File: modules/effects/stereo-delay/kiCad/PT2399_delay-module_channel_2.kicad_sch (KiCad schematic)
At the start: 38 parts, among them Q1 2N3904, U2 PT2399

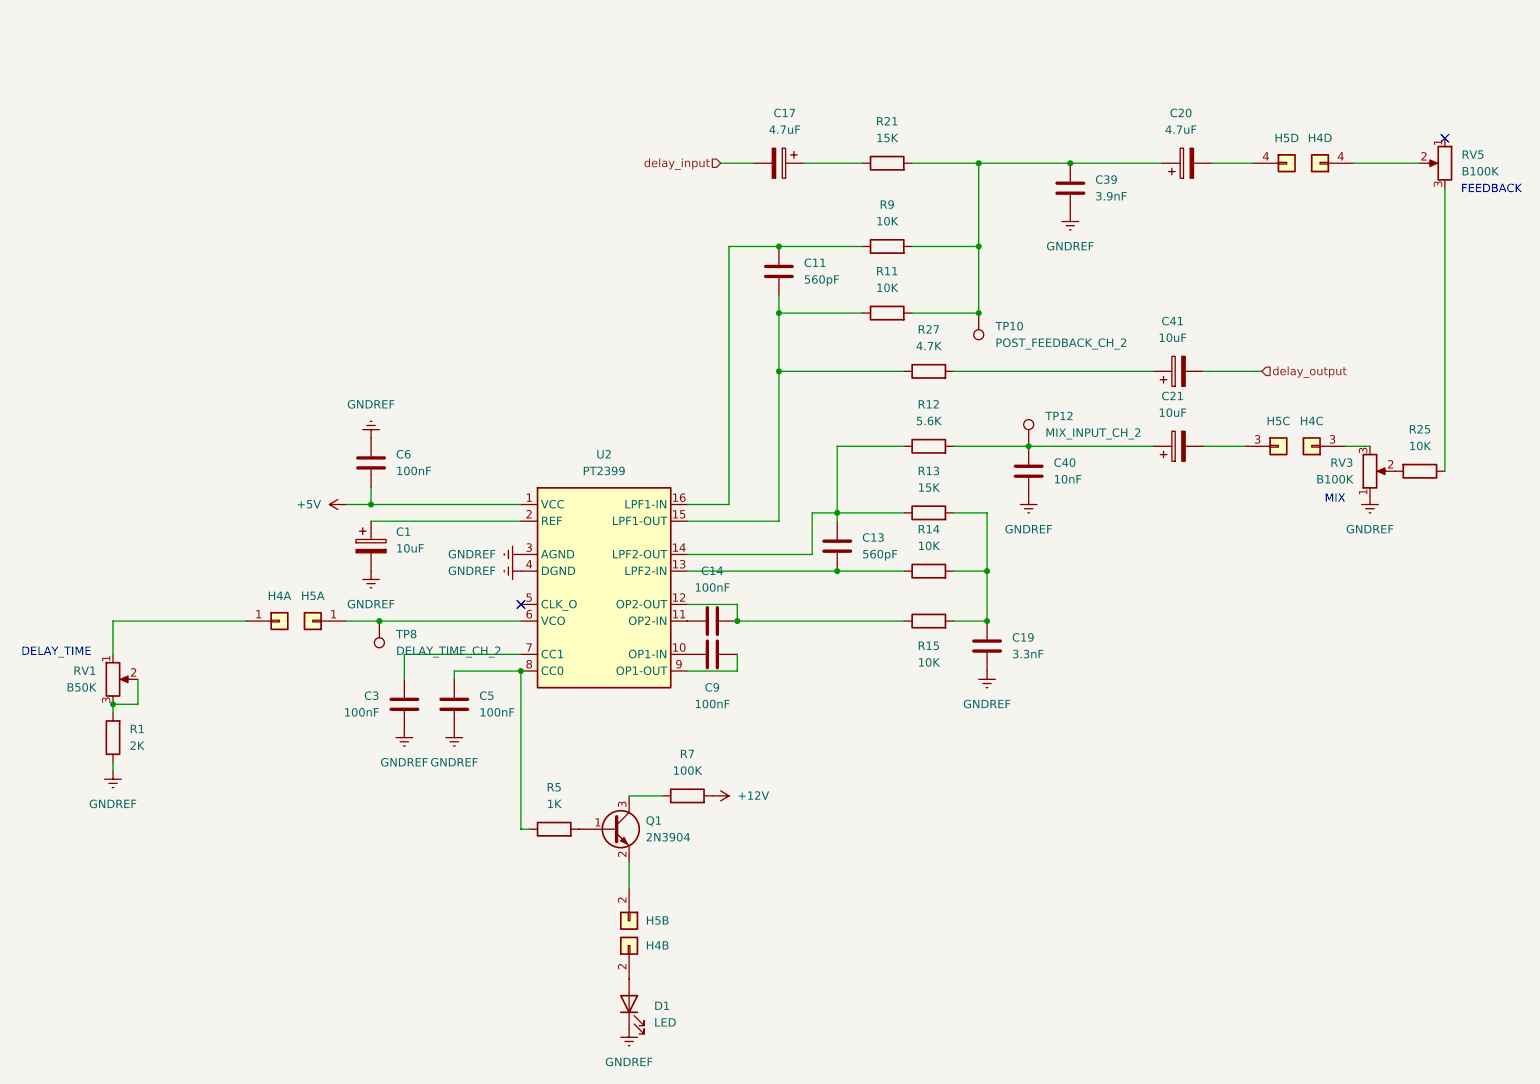
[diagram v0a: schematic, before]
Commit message: finish up PCB finals for run-2, continue on C code for midas/sequencer
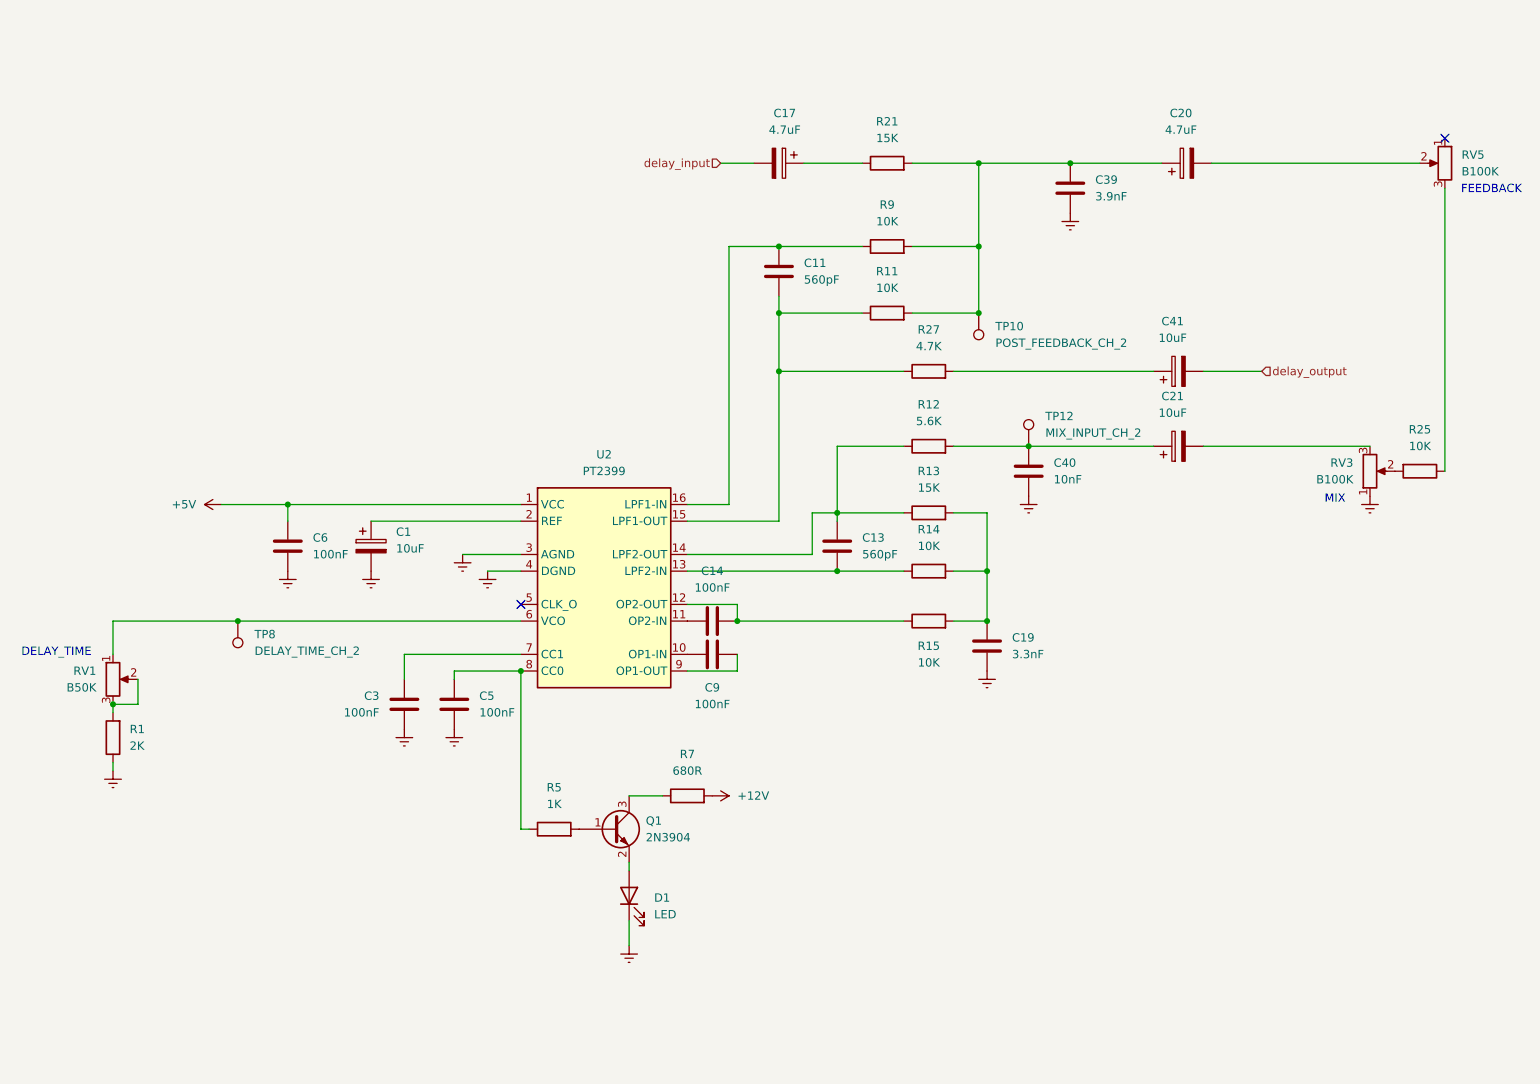
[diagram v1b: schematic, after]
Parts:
- removed H4: PinHeader_01x04, Synth:PinHeader_1x04_P2.54mm_Vertical, symbol synth:PinHeader_01x04
- removed H5: PinSocket_01x04, Synth:PinSocket_1x04_P2.54mm_Vertical, symbol synth:PinSocket_01x04
- R7: value 100K -> 680R
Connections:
- net +5V: now also C6.1; no longer C6.2
- net GNDREF: now also C6.2; no longer C6.1
- net at RV1.1: now also TP8.1, U2.6 (VCO)
- net at Q1.2 (E): now also D1.2 (A)
- net at RV5.2: now also C20.2
- net at RV3.3: now also C21.2
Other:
- moved on the sheet: C6, D1, TP8

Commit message: debugging and rework for ricochet, midas, wolkje. Added IBOM for drums and other modules.
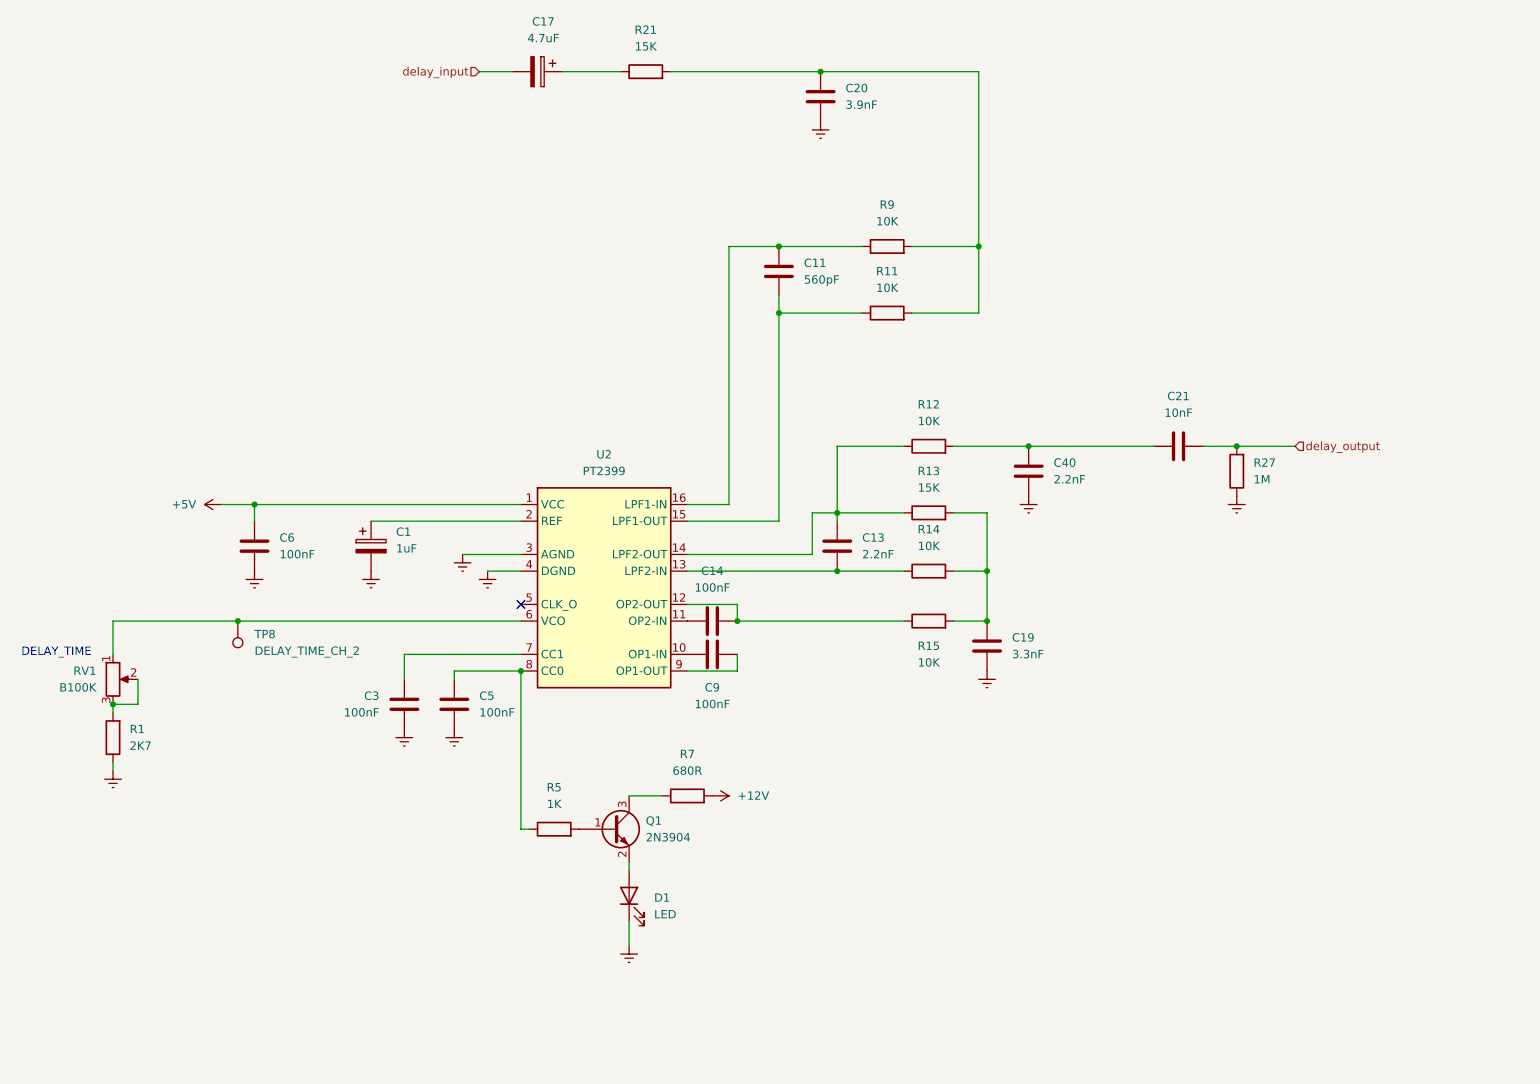
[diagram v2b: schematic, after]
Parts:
- removed C20: 4.7uF, Capacitor_THT:CP_Radial_D4.0mm_P2.00mm, symbol Device:C_Polarized
- removed C21, C41: 10uF, Capacitor_THT:CP_Radial_D4.0mm_P2.00mm, symbol Device:C_Polarized
- removed C39: 3.9nF, Capacitor_SMD:C_0805_2012Metric_Pad1.18x1.45mm_HandSolder, symbol Device:C
- removed R25: 10K, Resistor_SMD:R_0805_2012Metric_Pad1.20x1.40mm_HandSolder, symbol Device:R
- removed RV3, RV5: B100K, Synth:Potentiometer_TT_P0915N, symbol synth:R_Potentiometer (P0915N)
- removed TP10: POST_FEEDBACK_CH_2, Connector_Pin:Pin_D1.0mm_L10.0mm, symbol Connector:TestPoint
- removed TP12: MIX_INPUT_CH_2, Connector_Pin:Pin_D1.0mm_L10.0mm, symbol Connector:TestPoint
- added C20: 3.9nF, Capacitor_SMD:C_0805_2012Metric_Pad1.18x1.45mm_HandSolder, symbol Device:C
- added C21: 10nF, Capacitor_SMD:C_0805_2012Metric_Pad1.18x1.45mm_HandSolder, symbol Device:C
- C1: value 10uF -> 1uF
- C13: value 560pF -> 2.2nF
- C40: value 10nF -> 2.2nF
- R1: value 2K -> 2K7
- R12: value 5.6K -> 10K
- R27: value 4.7K -> 1M
- RV1: value B50K -> B100K
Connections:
- net GNDREF: now also R27.1, C20.2
- net delay_output: now also R27.2, C21.2
- net at C11.2, R11.1, U2.15 (LPF1-OUT): no longer R27.1
- net at C40.1, R12.2: now also C21.1
- net at R11.2, R21.2, R9.2: now also C20.1
- no-connect marks 2 -> 1
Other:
- note removed: "FEEDBACK"
- note removed: "MIX"
- moved on the sheet: C17, C6, R21
